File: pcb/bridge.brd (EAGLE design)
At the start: 104.2 x 63.6 mm, 38 parts, among them IC2 LM358D, IC3 78L05SMD, X1 PN61729-S

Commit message: bridge: Schematic beta version.
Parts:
- removed +12V: (no value), con-ptr500:AK500/2
- removed C10, C11: 22u, rcl:E2,5-6E
- removed C12, C13, C9: 100n, rcl:C1210
- removed D1, D2: 3V6, diode:DO34Z7
- removed IC3: 78L05SMD, linear:SO08
- removed ISP: (no value), pinhead:2X05
- removed R11, R12: 68, rcl:M1206
- removed R13: 1k5, rcl:M1206
- removed R14: 10k, rcl:M1206
- removed R15: 1k, rcl:M1206
- removed X1: PN61729-S, con-berg:PN61729-S
- added 12V: (no value), con-phoenix-350:1751248
- added C1, C2: 4u7, rcl:B/3528-21W
- added C3, C4: 100n, rcl:C1206
- added C5: 47u, rcl:C/6032-28W
- added U$1: ARDUINO_PRO_MICRO, sparkfun-boards:ARDUINO_PRO_MICRO
- RSENSE: device con-ptr500:AK500/2 -> con-phoenix-350:1751248
- moved BUS 62.0 mm to (4.76, 43.8), turned to 270 degrees
- moved R16 55.5 mm to (96.5, 39.4), turned to 270 degrees
- moved R4 37.3 mm to (51.4, 27.0), turned to 270 degrees
- moved R3 35.5 mm to (56.8, 24.4), turned to 0 degrees
- moved R8 32.4 mm to (55.9, 33.7), turned to 0 degrees
- moved S3 31.9 mm to (62.9, 9.84), turned to 90 degrees
- moved R6 26.3 mm to (55.2, 28.9), turned to 270 degrees
- moved C14 25.8 mm to (5.08, 32.1), turned to 270 degrees
- moved C7 25.4 mm to (52.4, 21.6), turned to 180 degrees
- moved R5 24.5 mm to (61.9, 27.6), turned to 270 degrees
- moved RSENSE 24.1 mm to (54.6, 6.99)
- moved S2 23.9 mm to (74.0, 9.84), turned to 90 degrees
- moved S1 22.9 mm to (85.4, 9.84), turned to 90 degrees
- moved C8 21.1 mm to (59.4, 28.6), turned to 90 degrees
- moved IC2 15.6 mm to (57.8, 16.5), turned to 90 degrees
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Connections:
- removed net N$3: LCD1.3, R14.1, R15.2
- removed net N$5: D2.C, R11.2, R13.1, X1.2
- removed net N$6: D1.C, R12.2, X1.3
- removed net PB0: LCD1.12
- removed net PB1: LCD1.13
- removed net PB2: LCD1.14
- removed net PB3: ISP.1
- removed net PB4: ISP.9
- removed net PB5: ISP.7
- removed net PC0: R7.2
- removed net PC1: C6.1, R1.1, R2.2
- removed net PC3: BUS.4, R10.1
- removed net PC4: BUS.3, R9.1
- removed net PC5: BUS.5, R8.1
- removed net PD0: S1.1, S1.2
- removed net PD1: S2.1, S2.2
- removed net PD2: S3.1, S3.2
- removed net PD3: R11.1
- removed net PD4: R12.1
- removed net PD5: LCD1.4
- removed net PD6: LCD1.6
- removed net PD7: LCD1.11
- removed net RESET: ISP.5
- new net ACURR: C2.+, C3.1, R7.2, U$1.12
- new net AVLTG: C1.+, C6.1, R1.1, R2.2, U$1.20
- new net BTN1: S3.1, S3.2, U$1.9
- new net BTN2: S2.1, S2.2, U$1.10
- new net BTN3: S1.1, S1.2, U$1.11
- new net DDB4: LCD1.11, U$1.16
- new net DDB5: LCD1.12, U$1.15
- new net DDB6: LCD1.13, U$1.14
- new net DDB7: LCD1.14, U$1.13
- new net DE: LCD1.6, U$1.17
- new net DRS: LCD1.4, U$1.19
- new net DRW: LCD1.5, U$1.18
- new net RX: U$1.2
- new net SCL: BUS.5, R8.1, U$1.6
- new net SDA: BUS.3, R9.1, U$1.5
- new net STOP: BUS.4, R10.1, U$1.7
- new net TX: U$1.1
- net +12V: now also 12V.1, U$1.24; no longer +12V.1, C13.2, IC3.8
- net +5V: now also C4.1, C5.+, U$1.21; no longer C10.+, C11.+, C12.2, C9.2, IC3.1, R13.2, R14.2
- net GND: now also 12V.2, C1.-, C2.-, C3.2, C4.2, C5.-, LCD1.3, U$1.23, U$1.3, U$1.4; no longer +12V.2, C10.-, C11.-, C12.1, C13.1, C9.1, D1.A, D2.A, IC3.2, IC3.3, IC3.6, IC3.7, ISP.10, ISP.4, ISP.6, ISP.8, LCD1.5, R15.1, X1.4, X1.S1, X1.S2
- net N$21: now also RSENSE.2; no longer RSENSE.1
- net N$29: now also RSENSE.1; no longer RSENSE.2
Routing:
- net +12V: track 153.2 -> 0.00 mm
- net +5V: track 148.3 -> 0.00 mm, vias 6 -> 0
- net GND: track 91.7 -> 0.00 mm, vias 2 -> 0
- net PD2: track 76.7 -> 0.00 mm, vias 2 -> 0
- net PD1: track 69.7 -> 0.00 mm, vias 2 -> 0
- net RESET: track 67.3 -> 0.00 mm, vias 4 -> 0
- net PB5: track 66.0 -> 0.00 mm
- net PD0: track 65.4 -> 0.00 mm, vias 2 -> 0
- net PB4: track 62.3 -> 0.00 mm
- net PB3: track 57.1 -> 0.00 mm
- net PC5: track 53.1 -> 0.00 mm
- net PC3: track 40.1 -> 0.00 mm
- net PC1: track 36.2 -> 0.00 mm, vias 2 -> 0
- net PC4: track 34.0 -> 0.00 mm
- net NET3: track 30.1 -> 0.00 mm
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- removed copper zone on layer 16, net GND
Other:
- board text removed: "Michal"
- board text removed: "SZARK"
- board text removed: "Slomkowski"

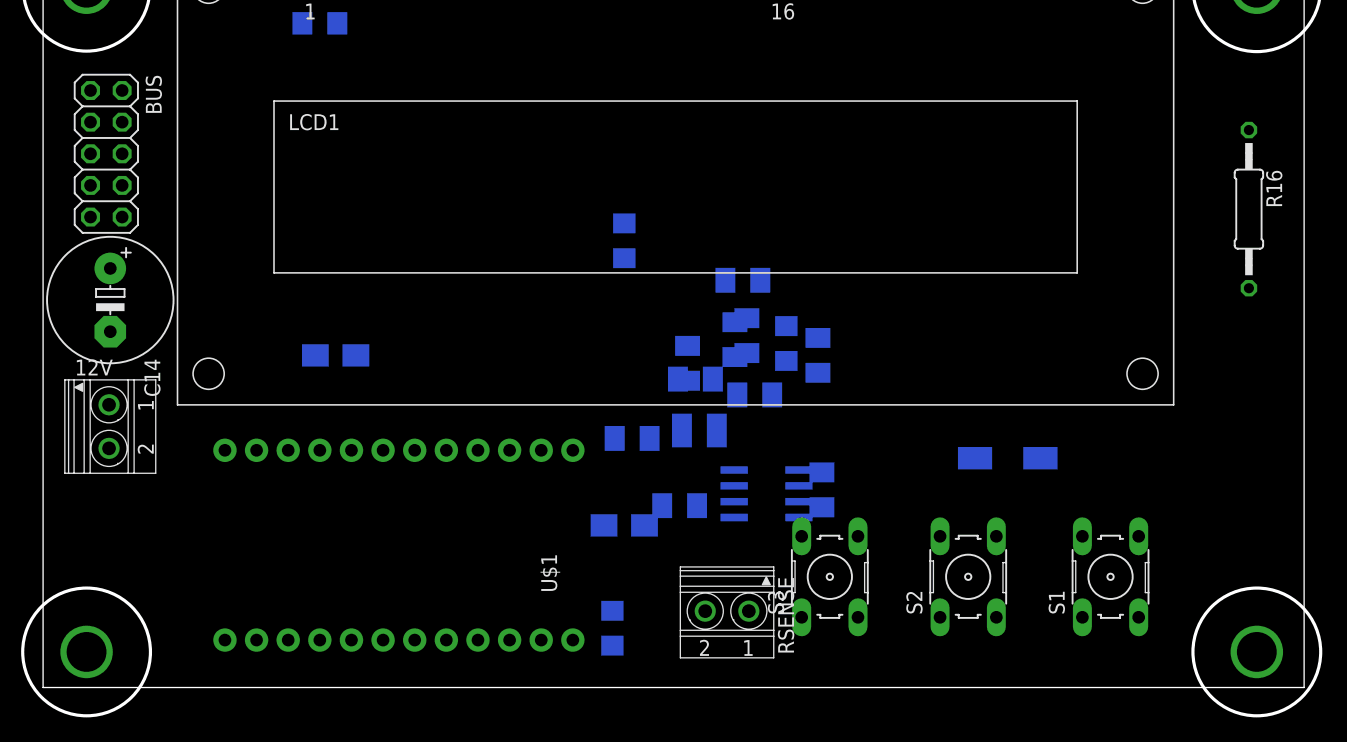
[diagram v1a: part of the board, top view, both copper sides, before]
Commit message: bridge: Update schematic positions and numbering.
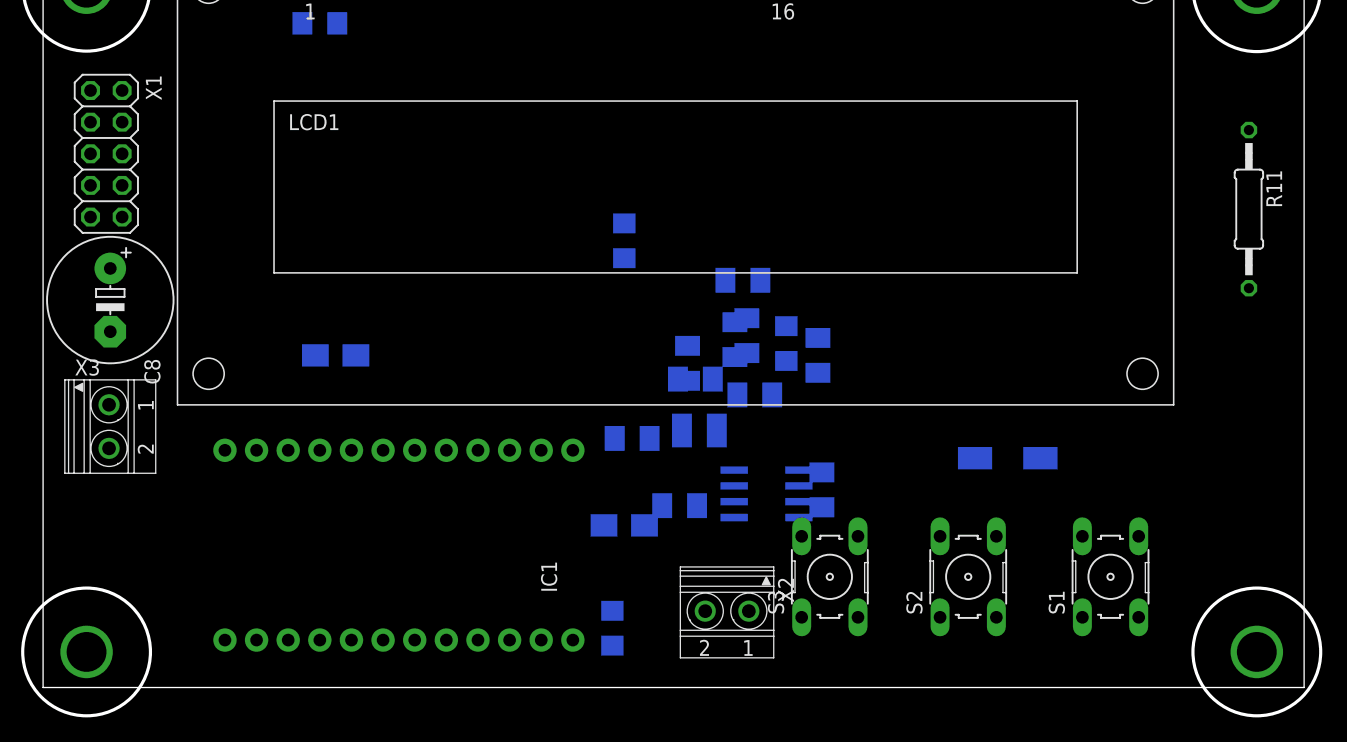
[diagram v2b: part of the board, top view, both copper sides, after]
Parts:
- removed C14: 470u, rcl:E5-10,5
- added C9: 100n, rcl:C1206
- C2: value 4u7 -> 100n; device rcl:B/3528-21W -> rcl:C1206
- C3: device rcl:C1206 -> rcl:C1210
- C5: value 47u -> 4u7; device rcl:C/6032-28W -> rcl:B/3528-21W
- C7: value 100n -> 47u; device rcl:C1210 -> rcl:C/6032-28W
- C8: value 100n -> 470u; device rcl:C1206 -> rcl:E5-10,5
- R10: value 2k2 -> 1k
- R3: value 8k2 -> 2k2
- R4: value 10k -> 4k7
- R5: value 8k2 -> 4k7
- R6: value 10k -> 8k2
- R7: value 100 -> 8k2
- R8, R9: value 4k7 -> 10k
- X1: value (none) -> SZARKBUS
- X2: value (none) -> RSENSE
- X3: value (none) -> +12V
- moved C8 54.4 mm to (5.08, 32.1), flipped to the top, turned to 270 degrees
- moved C4 45.4 mm to (59.4, 28.6), turned to 90 degrees
- moved C5 31.3 mm to (46.4, 14.0), turned to 180 degrees
- moved C6 31.1 mm to (45.4, 5.71)
- moved C7 24.9 mm to (77.2, 19.4), turned to 0 degrees
- moved C2 22.9 mm to (46.4, 36.8), turned to 90 degrees
- moved C3 17.3 mm to (52.4, 21.6), turned to 180 degrees
- moved R10 13.8 mm to (56.2, 29.2)
- moved R3 9.34 mm to (62.2, 16.8), turned to 90 degrees
- moved R5 8.53 mm to (55.9, 33.7), turned to 0 degrees
- moved R8 8.01 mm to (51.4, 27.0), turned to 270 degrees
- moved R7 5.93 mm to (61.9, 27.6), turned to 270 degrees
- moved R6 4.72 mm to (56.8, 24.4), turned to 0 degrees
- moved R9 4.49 mm to (55.2, 28.9), turned to 270 degrees
- moved R4 1.42 mm to (52.1, 25.7), turned to 180 degrees
- renumbered 12V to X3, BUS to X1, R16 to R11, RSENSE to X2, U$1 to IC1
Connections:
- net +12V: now also C8.+; no longer C14.+
- net +5V: now also C7.+, C9.1, R3.2, R4.2, R5.2; no longer C4.1, C5.+, R10.2, R8.2, R9.2
- net ACURR: now also C5.+, C6.1, R10.2; no longer C2.+, C3.1, R7.2
- net AVLTG: now also C2.1; no longer C6.1
- net GND: now also C2.2, C3.1, C7.-, C8.-, C9.2, R8.1; no longer C14.-, C2.-, C3.2, C4.2, C7.1, R4.1
- net N$1: now also C3.2, R6.2, R8.2; no longer C7.2, R3.2, R4.2
- net N$21: now also R7.1; no longer R5.1
- net N$29: now also R6.1; no longer R3.1
- net N$4: now also C4.2, R7.2, R9.1; no longer C8.2, R5.2, R6.1
- net NET3: now also C4.1, R10.1, R9.2; no longer C8.1, R6.2, R7.1
- net SCL: now also R5.1; no longer R8.1
- net SDA: now also R4.1; no longer R9.1
- net STOP: now also R3.1; no longer R10.1

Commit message: bridge: board shape.
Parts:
- moved C7 164.7 mm to (-77.5, 76.2), flipped to the top
- moved R7 151.3 mm to (-77.5, 86.4), flipped to the top, turned to 0 degrees
- moved R8 146.6 mm to (-82.5, 86.4), flipped to the top, turned to 0 degrees
- moved R6 143.3 mm to (-72.4, 86.4), flipped to the top
- moved S3 140.5 mm to (-61.0, 76.2), turned to 0 degrees
- moved S2 140.2 mm to (-49.5, 76.2), turned to 0 degrees
- moved S1 140.2 mm to (-38.1, 76.2), turned to 0 degrees
- moved R3 138.2 mm to (-57.1, 86.4), flipped to the top, turned to 0 degrees
- moved R11 137.3 mm to (-30.5, 91.4), turned to 0 degrees
- moved R5 134.0 mm to (-67.3, 86.4), flipped to the top
- moved C3 133.9 mm to (-69.8, 76.2), flipped to the top, turned to 0 degrees
- moved X2 132.9 mm to (-73.7, 41.9), turned to 0 degrees
- moved R4 129.4 mm to (-62.2, 86.4), flipped to the top, turned to 0 degrees
- moved R1 120.7 mm to (-47.0, 86.4), flipped to the top, turned to 0 degrees
- moved R2 118.7 mm to (-52.1, 86.4), flipped to the top, turned to 0 degrees
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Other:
- board size 104.2 x 63.6 mm -> 102.5 x 65.5 mm

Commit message: bridge: Mock PCB ready.
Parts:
- added C10: 100n, rcl:C1206
- C8: device rcl:E5-10,5 -> rcl:E5-8,5
- moved S3 167.2 mm to (95.2, 16.5), turned to 90 degrees
- moved C1 148.6 mm to (52.1, 19.1), flipped to the bottom, turned to 90 degrees
- moved S2 146.1 mm to (83.8, 16.5), turned to 90 degrees
- moved R5 136.0 mm to (47.0, 12.7), flipped to the bottom, turned to 90 degrees
- moved R11 135.9 mm to (96.5, 43.2), turned to 270 degrees
- moved R3 130.7 mm to (50.8, 12.7), flipped to the bottom, turned to 90 degrees
- moved R4 128.6 mm to (43.2, 12.7), flipped to the bottom, turned to 90 degrees
- moved S1 125.6 mm to (72.4, 16.5), turned to 90 degrees
- moved C7 118.9 mm to (25.4, 16.5), flipped to the bottom, turned to 180 degrees
- moved R2 117.7 mm to (44.5, 19.1), flipped to the bottom, turned to 90 degrees
- moved R8 117.0 mm to (14.0, 20.3), flipped to the bottom, turned to 90 degrees
- moved LCD1 108.7 mm to (21.6, 61.0)
- moved R1 108.7 mm to (39.4, 20.3), flipped to the bottom
- moved R7 104.6 mm to (14.0, 35.6), flipped to the bottom, turned to 180 degrees
- moved C3 103.9 mm to (17.8, 20.3), flipped to the bottom, turned to 90 degrees
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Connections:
- net +5V: now also C10.1
- net ACURR: now also IC1.19; no longer IC1.12
- net DDB4: now also IC1.15; no longer IC1.16
- net DDB5: now also IC1.14; no longer IC1.15
- net DDB6: now also IC1.13; no longer IC1.14
- net DDB7: now also IC1.12; no longer IC1.13
- net DE: now also IC1.16; no longer IC1.17
- net DRS: now also IC1.18; no longer IC1.19
- net DRW: now also IC1.17; no longer IC1.18
- net GND: now also C10.2
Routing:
- net GND: track 0.00 -> 340.0 mm
- net +12V: track 0.00 -> 152.6 mm, vias 0 -> 8
- net +5V: track 0.00 -> 140.5 mm, vias 0 -> 4
- net DDB7: track 0.00 -> 62.2 mm, vias 0 -> 2
- net BTN1: track 0.00 -> 54.2 mm
- net SDA: track 0.00 -> 48.9 mm
- net DRW: track 0.00 -> 45.2 mm
- net DRS: track 0.00 -> 45.2 mm
- net DE: track 0.00 -> 45.2 mm
- net N$2: track 0.00 -> 44.1 mm
- net STOP: track 0.00 -> 44.0 mm
- net DDB6: track 0.00 -> 41.0 mm
- net DDB5: track 0.00 -> 41.0 mm
- net DDB4: track 0.00 -> 41.0 mm
- net BTN2: track 0.00 -> 39.2 mm
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
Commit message: bridge: Board ready beta.
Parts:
- added C11: 100n, rcl:C1206
- C10: value 100n -> 470u; device rcl:C1206 -> rcl:E5-8,5
- C7: value 47u -> 100n; device rcl:C/6032-28W -> rcl:C1206
- C8: value 470u -> 47u; device rcl:E5-8,5 -> rcl:C/6032-28W
- moved C9 34.5 mm to (26.7, 24.1), turned to 270 degrees
- moved C8 31.4 mm to (26.7, 16.5), flipped to the bottom, turned to 180 degrees
- moved C10 25.9 mm to (5.71, 39.4), flipped to the top
- moved C7 18.2 mm to (40.0, 27.3), turned to 0 degrees
- moved R7 5.75 mm to (19.7, 36.2)
- moved R6 2.01 mm to (9.53, 23.5)
- moved C3 1.91 mm to (17.8, 22.2)
- moved R8 1.91 mm to (14.0, 22.2)
- moved R1 1.27 mm to (39.4, 19.1)
- moved R10 1.27 mm to (29.2, 33.0)
- moved R9 1.27 mm to (22.9, 33.0)
- moved C5 0.64 mm to (37.5, 33.0)
- moved C4 0.64 mm to (22.9, 29.8)
- moved X1 0.63 mm to (20.3, 5.71)
- moved R11 0.63 mm to (95.9, 43.2)
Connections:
- net +12V: now also C10.+; no longer C8.+
- net +5V: now also C11.1, C7.1, C8.+; no longer C10.1, C7.+
- net GND: now also C10.-, C11.2, C7.2; no longer C10.2, C7.-
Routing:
- net GND: track 340.0 -> 98.2 mm
- net +5V: track 140.5 -> 93.7 mm, vias 4 -> 2
- net N$21: track 7.69 -> 14.0 mm
- net N$4: track 15.9 -> 9.94 mm
- net SDA: track 48.9 -> 53.5 mm
- net +12V: track 152.6 -> 148.1 mm
- net DRW: track 45.2 -> 48.6 mm
- net DE: track 45.2 -> 48.6 mm
- net DRS: track 45.2 -> 48.6 mm
- net DDB7: track 62.2 -> 65.0 mm
- net N$29: track 7.41 -> 4.66 mm
- net BTN3: track 27.3 -> 24.7 mm
- net STOP: track 44.0 -> 45.7 mm
- net SCL: track 32.2 -> 33.6 mm
- net NET3: track 11.4 -> 10.2 mm
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- added copper zone on layer 16, net GND
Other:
- board size 102.5 x 65.5 mm -> 102.5 x 66 mm
- board text added: "(C) 2014 Michal"
- board text added: "3"
- board text added: "SZARK"
- board text added: "Slomkowski"
- board text added: "Version"
